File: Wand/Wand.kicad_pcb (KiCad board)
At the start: 4 copper layers, 50 x 7 mm, 20 parts, among them P1 ISP, P2 KLB4, P3 BASE, U1 ATMEGA328-MMH, U2 MAX31855KASA+, U3 MPU-6050

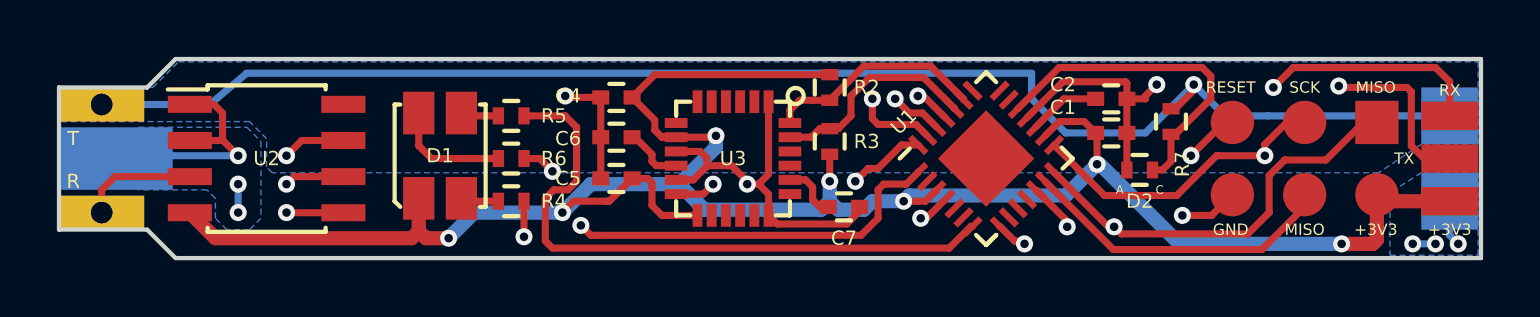
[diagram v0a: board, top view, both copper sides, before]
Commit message: Changed 0402 to sod-523 for Zener
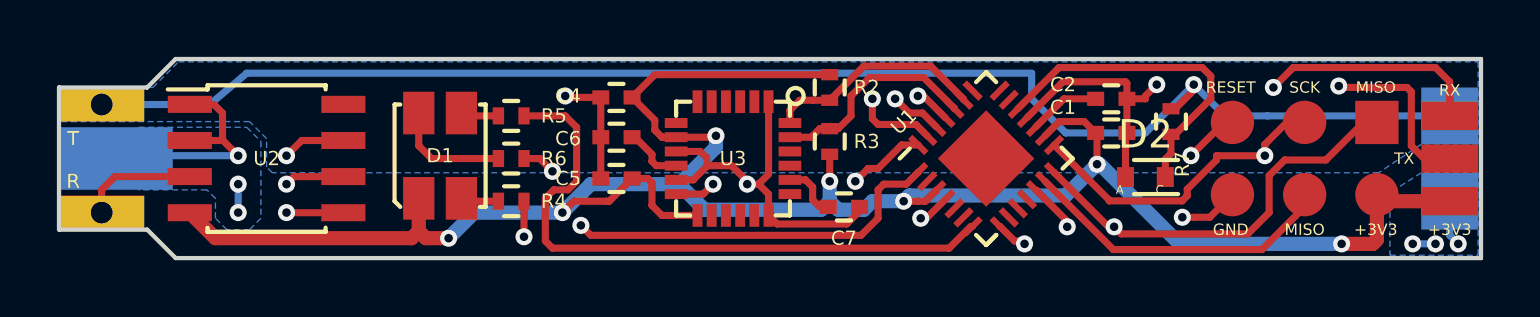
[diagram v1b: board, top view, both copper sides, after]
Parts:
- D2: footprint Resistors_SMD:R_0402 -> Diodes_SMD:SOD-523
- moved D2 0.32 mm to (135.2, 112.7), turned to 0 degrees
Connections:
- U1 pad 10: Net-(U1-Pad10) -> (no net)
- U1 pad 11: Net-(U1-Pad11) -> (no net)
- U1 pad 2: Net-(U1-Pad2) -> (no net)
- U1 pad 20: Net-(U1-Pad20) -> (no net)
- U1 pad 21: Net-(U1-Pad21) -> (no net)
- U1 pad 22: Net-(U1-Pad22) -> (no net)
- U1 pad 5: Net-(U1-Pad5) -> (no net)
- U1 pad 6: Net-(U1-Pad6) -> (no net)
- U1 pad 9: Net-(U1-Pad9) -> (no net)
- U2 pad 8: Net-(U2-Pad8) -> (no net)
- U3 pad 14: Net-(U3-Pad14) -> (no net)
- U3 pad 15: Net-(U3-Pad15) -> (no net)
- U3 pad 16: Net-(U3-Pad16) -> (no net)
- U3 pad 17: Net-(U3-Pad17) -> (no net)
- U3 pad 19: Net-(U3-Pad19) -> (no net)
- U3 pad 2: Net-(U3-Pad2) -> (no net)
- U3 pad 21: Net-(U3-Pad21) -> (no net)
- U3 pad 22: Net-(U3-Pad22) -> (no net)
- U3 pad 3: Net-(U3-Pad3) -> (no net)
- U3 pad 4: Net-(U3-Pad4) -> (no net)
- U3 pad 5: Net-(U3-Pad5) -> (no net)
- U3 pad 6: Net-(U3-Pad6) -> (no net)
- U3 pad 7: Net-(U3-Pad7) -> (no net)

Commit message: Finished change for 0402, also generated fabrication data
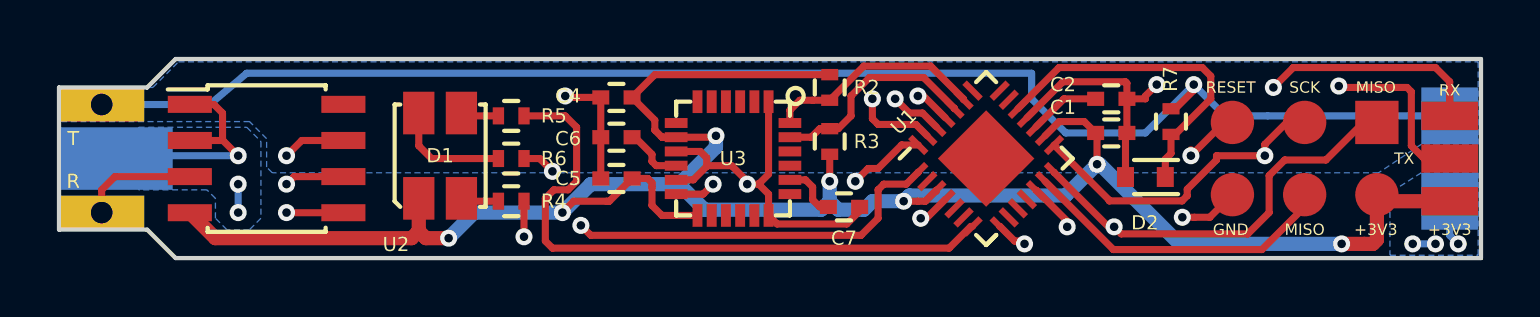
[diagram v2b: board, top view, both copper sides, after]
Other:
- board text removed: "A"
- board text removed: "C"
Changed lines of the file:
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@@
     (links 57)
     (no_connects 0)
-    (area 96.924999 108.424999 147.075001 115.575001)
+    (area 83.414287 99.5125 161.985715 132.377185)
     (thickness 1.6)
-    (drawings 35)
+    (drawings 33)
     (tracks 393)
     (zones 0)
@@
   )
   (layers
-    (0 F.Signal.Cu signal)
-    (1 In1.Ground.Cu power)
-    (2 In2.Signal.Cu signal)
-    (31 B.Power.Cu mixed)
-    (32 B.Adhes user)
-    (33 F.Adhes user)
-    (34 B.Paste user)
-    (35 F.Paste user)
+    (0 F.Signal.Cu signal hide)
+    (1 In1.Ground.Cu power hide)
+    (2 In2.Signal.Cu signal hide)
+    (31 B.Power.Cu mixed hide)
+    (32 B.Adhes user hide)
+    (33 F.Adhes user hide)
+    (34 B.Paste user hide)
+    (35 F.Paste user hide)
     (36 B.SilkS user hide)
-    (37 F.SilkS user hide)
-    (38 B.Mask user)
+    (37 F.SilkS user)
+    (38 B.Mask user hide)
     (39 F.Mask user)
-    (40 Dwgs.User user)
-    (41 Cmts.User user)
-    (42 Eco1.User user)
-    (43 Eco2.User user)
+    (40 Dwgs.User user hide)
+    (41 Cmts.User user hide)
+    (42 Eco1.User user hide)
+    (43 Eco2.User user hide)
     (44 Edge.Cuts user)
     (45 Margin user)
     (46 B.CrtYd user)
     (47 F.CrtYd user)
-    (48 B.Fab user)
-    (49 F.Fab user)
+    (48 B.Fab user hide)
+    (49 F.Fab user hide)
   )
   (setup
@@
     (pcb_text_size 1.5 1.5)
     (mod_edge_width 0.15)
-    (mod_text_size 1 1)
-    (mod_text_width 0.15)
+    (mod_text_size 0.5 0.5)
+    (mod_text_width 0.125)
     (pad_size 1.524 1.524)
     (pad_drill 0.762)
     (pad_to_mask_clearance 0.2)
     (aux_axis_origin 0 0)
-    (visible_elements 7FFEFFFF)
+    (visible_elements 7FFEFF3F)
     (pcbplotparams
-      (layerselection 0x010f8_80000007)
-      (usegerberextensions false)
+      (layerselection 0x010f8_ffffffff)
+      (usegerberextensions true)
       (excludeedgelayer true)
       (linewidth 0.100000)
-      (plotframeref true)
+      (plotframeref false)
       (viasonmask false)
       (mode 1)
@@
       (drillshape 0)
       (scaleselection 1)
-      (outputdirectory Production/))
+      (outputdirectory ProductionProtel/))
   )
   (net 0 "")
@@
     )
     (fp_text value BASE (at 4.6 -11.8) (layer F.Fab)
-      (effects (font (size 1 1) (thickness 0.15)))
+      (effects (font (size 0.5 0.5) (thickness 0.125)))
     )
     (pad 2 smd rect (at 0 -1.5) (size 2 2) (layers B.Power.Cu B.Paste B.Mask)
@@
     )
     (fp_text value MPU-6050 (at 2.8194 -3.8608 270) (layer F.Fab)
-      (effects (font (size 1 1) (thickness 0.15)))
+      (effects (font (size 0.5 0.5) (thickness 0.125)))
     )
     (fp_circle (center -2.2 -2.2) (end -2 -2) (layer F.SilkS) (width 0.15))
@@
     (tags "SOIC 1.27")
     (attr smd)
-    (fp_text reference U2 (at 0 0) (layer F.SilkS)
+    (fp_text reference U2 (at 4.55 3.02) (layer F.SilkS)
       (effects (font (size 0.5 0.5) (thickness 0.125)))
     )
     (fp_text value MAX31855KASA+ (at 0 3.5) (layer F.Fab)
-      (effects (font (size 1 1) (thickness 0.15)))
+      (effects (font (size 0.5 0.5) (thickness 0.125)))
     )
     (fp_line (start -3.75 -2.75) (end -3.75 2.75) (layer F.CrtYd) (width 0.05))
@@
     )
     (fp_text value ATMEGA328-MMH (at 4.617407 -4.70226 225) (layer F.Fab)
-      (effects (font (size 1 1) (thickness 0.15)))
+      (effects (font (size 0.5 0.5) (thickness 0.125)))
     )
     (fp_line (start -1.65 2.15) (end -2.15 2.15) (layer F.SilkS) (width 0.15))
@@
     )
     (fp_text value 10R (at 0 1.8 180) (layer F.Fab)
-      (effects (font (size 1 1) (thickness 0.15)))
+      (effects (font (size 0.5 0.5) (thickness 0.125)))
     )
     (fp_line (start -0.95 -0.65) (end 0.95 -0.65) (layer F.CrtYd) (width 0.05))
@@
     )
     (fp_text value 10R (at 0 1.8 180) (layer F.Fab)
-      (effects (font (size 1 1) (thickness 0.15)))
+      (effects (font (size 0.5 0.5) (thickness 0.125)))
     )
     (fp_line (start -0.95 -0.65) (end 0.95 -0.65) (layer F.CrtYd) (width 0.05))
@@
     )
     (fp_text value 68R (at 0 1.8 180) (layer F.Fab)
-      (effects (font (size 1 1) (thickness 0.15)))
+      (effects (font (size 0.5 0.5) (thickness 0.125)))
     )
     (fp_line (start -0.95 -0.65) (end 0.95 -0.65) (layer F.CrtYd) (width 0.05))
@@
     )
     (fp_text value 10k (at 0 1.8 90) (layer F.Fab)
-      (effects (font (size 1 1) (thickness 0.15)))
+      (effects (font (size 0.5 0.5) (thickness 0.125)))
     )
     (fp_line (start -0.95 -0.65) (end 0.95 -0.65) (layer F.CrtYd) (width 0.05))
@@
     )
     (fp_text value 10k (at 0 1.8 270) (layer F.Fab)
-      (effects (font (size 1 1) (thickness 0.15)))
+      (effects (font (size 0.5 0.5) (thickness 0.125)))
     )
     (fp_line (start -0.95 -0.65) (end 0.95 -0.65) (layer F.CrtYd) (width 0.05))
@@
     )
     (fp_text value KLB4 (at 0 3.9) (layer B.Fab)
-      (effects (font (size 1 1) (thickness 0.15)) (justify mirror))
+      (effects (font (size 0.5 0.5) (thickness 0.125)) (justify mirror))
     )
     (pad T thru_hole rect (at 0 -1.9) (size 3 1.2) (drill 0.762) (layers *.Cu *.Mask B.SilkS)
@@
     )
     (fp_text value 2.2n (at 0 1.7 180) (layer F.Fab)
-      (effects (font (size 1 1) (thickness 0.15)))
+      (effects (font (size 0.5 0.5) (thickness 0.125)))
     )
     (fp_line (start -1.15 -0.6) (end 1.15 -0.6) (layer F.CrtYd) (width 0.05))
@@
     )
     (fp_text value 100n (at 0 1.7) (layer F.Fab)
-      (effects (font (size 1 1) (thickness 0.15)))
+      (effects (font (size 0.5 0.5) (thickness 0.125)))
     )
     (fp_line (start -1.15 -0.6) (end 1.15 -0.6) (layer F.CrtYd) (width 0.05))
@@
     )
     (fp_text value 10n (at 0 1.7) (layer F.Fab)
-      (effects (font (size 1 1) (thickness 0.15)))
+      (effects (font (size 0.5 0.5) (thickness 0.125)))
     )
     (fp_line (start -1.15 -0.6) (end 1.15 -0.6) (layer F.CrtYd) (width 0.05))
@@
     )
     (fp_text value 100n (at 0 1.7) (layer F.Fab)
-      (effects (font (size 1 1) (thickness 0.15)))
+      (effects (font (size 0.5 0.5) (thickness 0.125)))
     )
     (fp_line (start -1.15 -0.6) (end 1.15 -0.6) (layer F.CrtYd) (width 0.05))
@@
     )
     (fp_text value 100n (at 0 1.7) (layer F.Fab)
-      (effects (font (size 1 1) (thickness 0.15)))
+      (effects (font (size 0.5 0.5) (thickness 0.125)))
     )
     (fp_line (start -1.15 -0.6) (end 1.15 -0.6) (layer F.CrtYd) (width 0.05))
@@
     )
     (fp_text value 100n (at 0 1.7) (layer F.Fab)
-      (effects (font (size 1 1) (thickness 0.15)))
+      (effects (font (size 0.5 0.5) (thickness 0.125)))
     )
     (fp_line (start -1.15 -0.6) (end 1.15 -0.6) (layer F.CrtYd) (width 0.05))
@@
     )
     (fp_text value ASMB-MTB0-0A3A2 (at 0 -3.2) (layer F.Fab)
-      (effects (font (size 1 1) (thickness 0.15)))
+      (effects (font (size 0.5 0.5) (thickness 0.125)))
     )
     (fp_line (start 1.4 -1.8) (end 1.6 -1.8) (layer F.SilkS) (width 0.15))
@@
     )
     (fp_text value ISP (at 0 1.2 360) (layer F.Fab)
-      (effects (font (size 0.6 0.6) (thickness 0.15)))
+      (effects (font (size 0.5 0.5) (thickness 0.125)))
     )
     (pad 1 connect rect (at -1.27 -2.54 270) (size 1.524 1.524) (layers F.Signal.Cu F.Mask)
@@
     (tags "resistor 0402")
     (attr smd)
-    (fp_text reference R7 (at 1.5 -0.4 270) (layer F.SilkS)
+    (fp_text reference R7 (at -1.5 0.02 270) (layer F.SilkS)
       (effects (font (size 0.5 0.5) (thickness 0.125)))
     )
     (fp_text value 10K (at 0 1.8 270) (layer F.Fab)
-      (effects (font (size 1 1) (thickness 0.15)))
+      (effects (font (size 0.5 0.5) (thickness 0.125)))
     )
     (fp_line (start -0.95 -0.65) (end 0.95 -0.65) (layer F.CrtYd) (width 0.05))
@@
     (tags "Diode SOD523")
     (attr smd)
-    (fp_text reference D2 (at 0 -1.5) (layer F.SilkS)
-      (effects (font (size 1 1) (thickness 0.15)))
+    (fp_text reference D2 (at -0.02 1.61) (layer F.SilkS)
+      (effects (font (size 0.5 0.5) (thickness 0.125)))
     )
     (fp_text value 3V3 (at 0 1.7) (layer F.Fab)
-      (effects (font (size 1 1) (thickness 0.15)))
+      (effects (font (size 0.5 0.5) (thickness 0.125)))
     )
     (fp_line (start -0.4 0.6) (end 1.15 0.6) (layer F.SilkS) (width 0.15))
@@
       (net 24 /HEAT_DETECT))
   )
-  (gr_text C (at 135.7 113.1) (layer F.SilkS)
-    (effects (font (size 0.3 0.3) (thickness 0.075)))
-  )
-  (gr_text A (at 134.3 113.1) (layer F.SilkS)
-    (effects (font (size 0.3 0.3) (thickness 0.075)))
-  )
   (gr_text R (at 100.5 113.9) (layer B.SilkS)
